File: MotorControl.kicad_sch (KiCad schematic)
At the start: 14 parts, among them J5 Conn_01x03_Pin, U3 CSD18534Q5A, U4 CSD18534Q5A, U5 CSD18534Q5A, U6 CSD18534Q5A, U7 CSD18534Q5A, U8 CSD18534Q5A, U9 DRV8323HRTAR

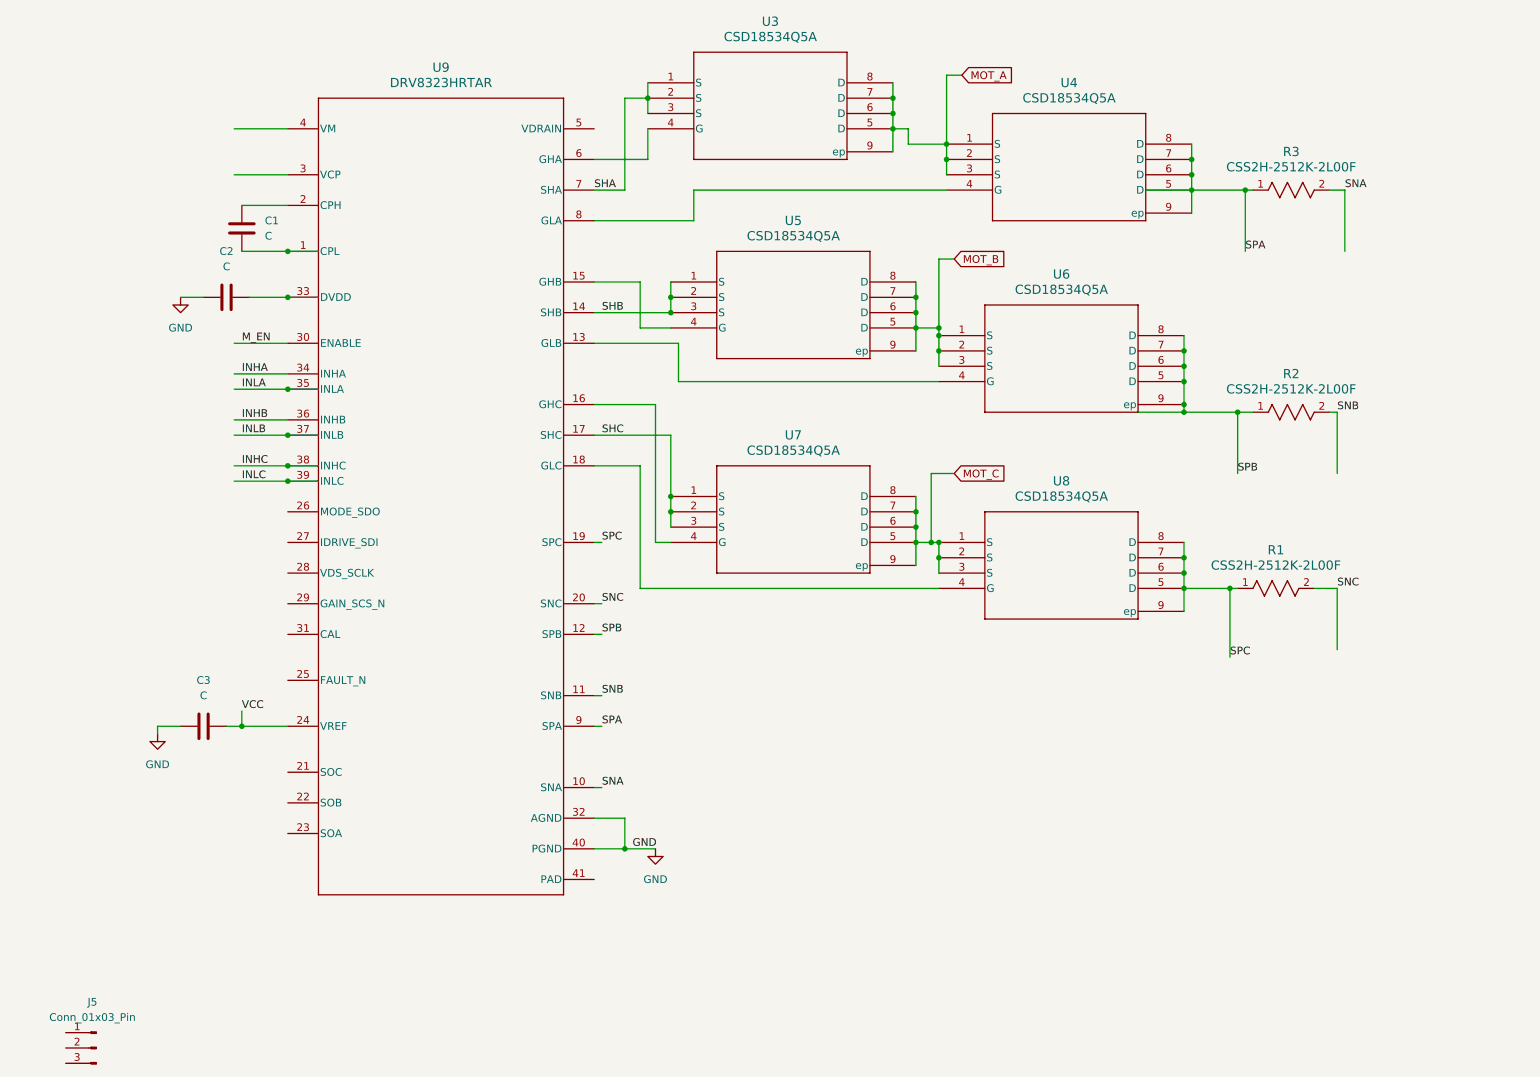
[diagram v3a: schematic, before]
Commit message: using vias on SNA/SPA instead of GxA b/c switching speed
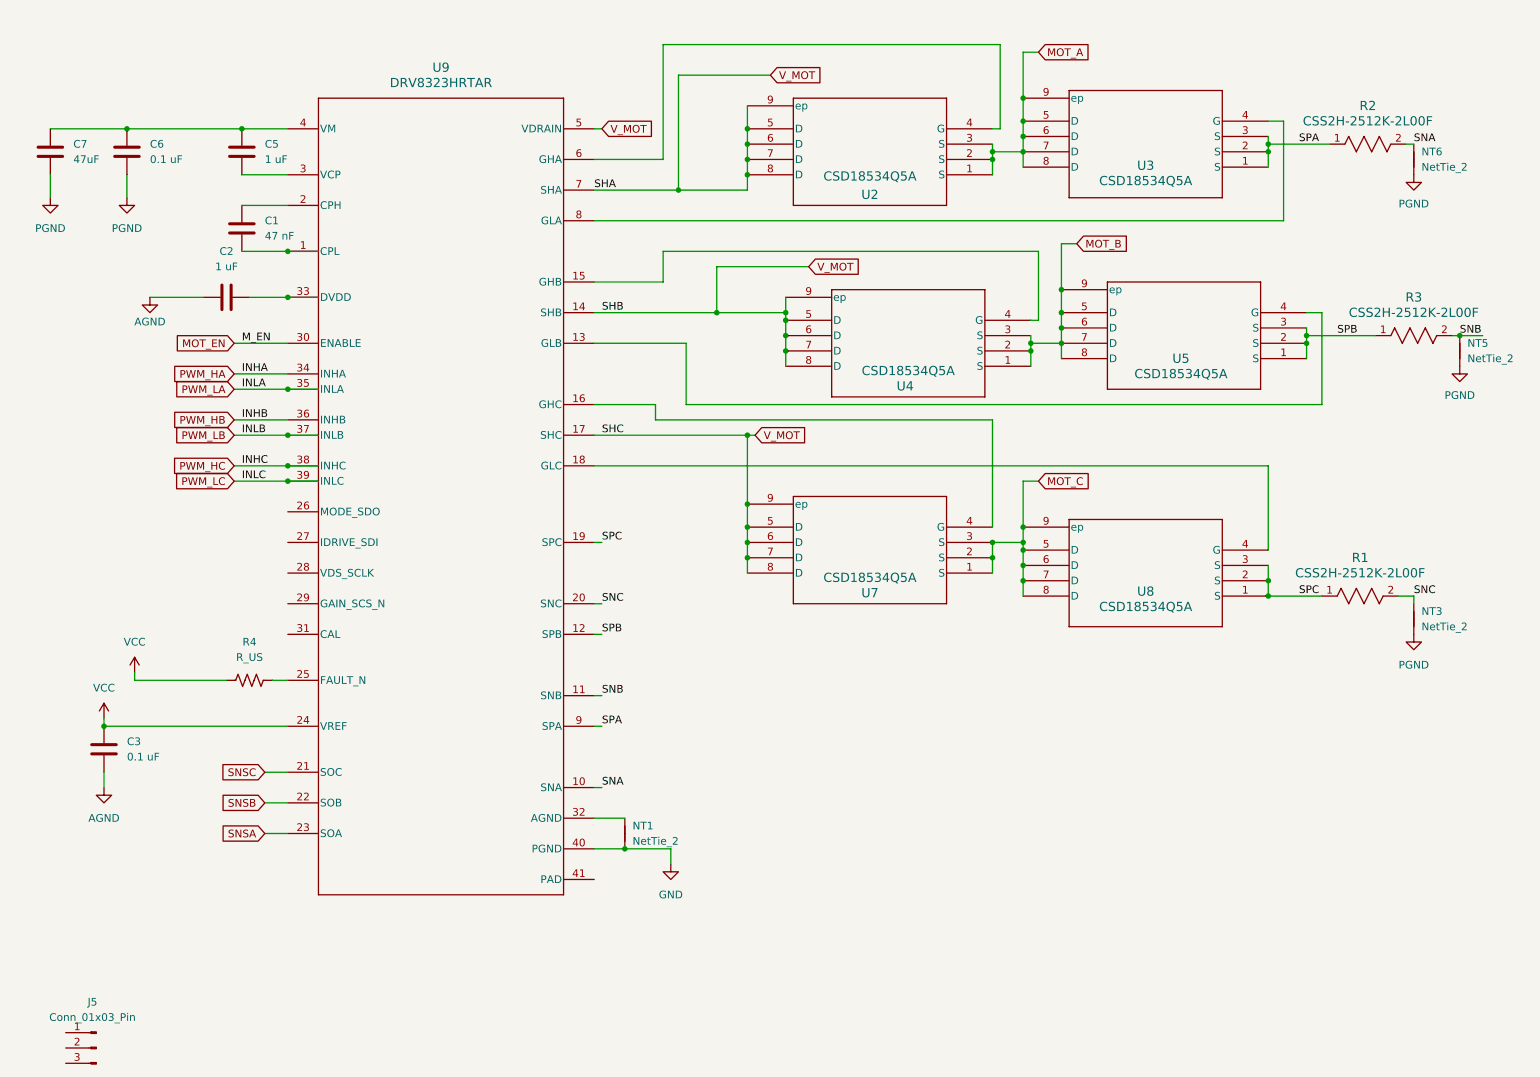
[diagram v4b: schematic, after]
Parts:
- removed U6: CSD18534Q5A, DQJ8, symbol CSD18534Q5A:CSD18534Q5A
- added C5: 1 uF, symbol Device:C
- added C6: 0.1 uF, symbol Device:C
- added C7: 47uF, symbol Device:C
- added NT1, NT3, NT5, NT6: NetTie_2, symbol Device:NetTie_2
- added R4: R_US, symbol Device:R_US
- added U2: CSD18534Q5A, DQJ8, symbol CSD18534Q5A:CSD18534Q5A
- C1: value C -> 47 nF
- C2: value C -> 1 uF
- C3: value C -> 0.1 uF
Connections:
- net GND: now also NT1.1; no longer C2.1, C3.1, U9.32 (AGND)
- net MOT_A: now also U2.1 (S), U2.2 (S), U2.3 (S); no longer U4.1 (S), U4.2 (S), U4.3 (S)
- net MOT_B: now also U4.1 (S), U4.2 (S), U4.3 (S)
- net MOT_C: now also U7.1 (S), U7.2 (S), U7.3 (S), U8.5 (D), U8.6 (D), U8.7 (D), U8.8 (D), U8.9 (ep); no longer U7.5 (D), U7.6 (D), U7.7 (D), U7.8 (D), U7.9 (ep), U8.1 (S), U8.2 (S), U8.3 (S)
- net SNA: now also R2.2, NT6.1; no longer R3.2
- net SNB: now also R3.2, NT5.1; no longer R2.2
- net SNC: now also NT3.1
- net SPA: now also R2.1, U3.1 (S), U3.2 (S), U3.3 (S); no longer R3.1, U4.5 (D), U4.6 (D), U4.7 (D), U4.8 (D), U4.9 (ep)
- net SPB: now also R3.1, U5.1 (S), U5.2 (S), U5.3 (S); no longer R2.1
- net SPC: now also U8.1 (S), U8.2 (S), U8.3 (S); no longer U8.5 (D), U8.6 (D), U8.7 (D), U8.8 (D), U8.9 (ep)
- net VCC: now also R4.1
- net at U5.4 (G): now also U9.13 (GLB); no longer U9.15 (GHB)
- net SNSC: now reaches U9.21 (SOC)
- net SNSB: now reaches U9.22 (SOB)
- net SNSA: now reaches U9.23 (SOA)
- net at U9.25 (FAULT_N): now also R4.2
- net at U9.3 (VCP): now also C5.2
- net at U9.4 (VM): now also C5.1, C6.1, C7.1
- net V_MOT: now reaches U9.5 (VDRAIN)
- net V_MOT: now also U4.5 (D), U4.6 (D), U4.7 (D), U4.8 (D), U4.9 (ep), U7.5 (D), U7.6 (D), U7.7 (D), U7.8 (D), U7.9 (ep), U9.14 (SHB), U9.17 (SHC), U9.7 (SHA), U2.5 (D), U2.6 (D), U2.7 (D), U2.8 (D), U2.9 (ep)
- net at U3.4 (G): now also U9.8 (GLA); no longer U9.6 (GHA)
- net at U4.4 (G): now also U9.15 (GHB); no longer U9.8 (GLA)
- net INHA renamed PWM_HA
- net INHB renamed PWM_HB
- net INHC renamed PWM_HC
- net INLA renamed PWM_LA
- net INLB renamed PWM_LB
- net INLC renamed PWM_LC
- net M_EN renamed MOT_EN
- removed net SHA: U3.1 (S), U3.2 (S), U3.3 (S), U9.7 (SHA)
- removed net SHB: U5.1 (S), U5.2 (S), U5.3 (S), U9.14 (SHB)
- removed net SHC: U7.1 (S), U7.2 (S), U7.3 (S), U9.17 (SHC)
- new net: NT1.2, U9.32 (AGND)
- new net: U2.4 (G), U9.6 (GHA)
- new net AGND: C2.1, C3.1
- new net PGND: C6.2, C7.2, NT3.2, NT5.2, NT6.2
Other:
- moved on the sheet: C3, R1, U7, U8

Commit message: full gate reroute with zones and sense lines like the layout guide
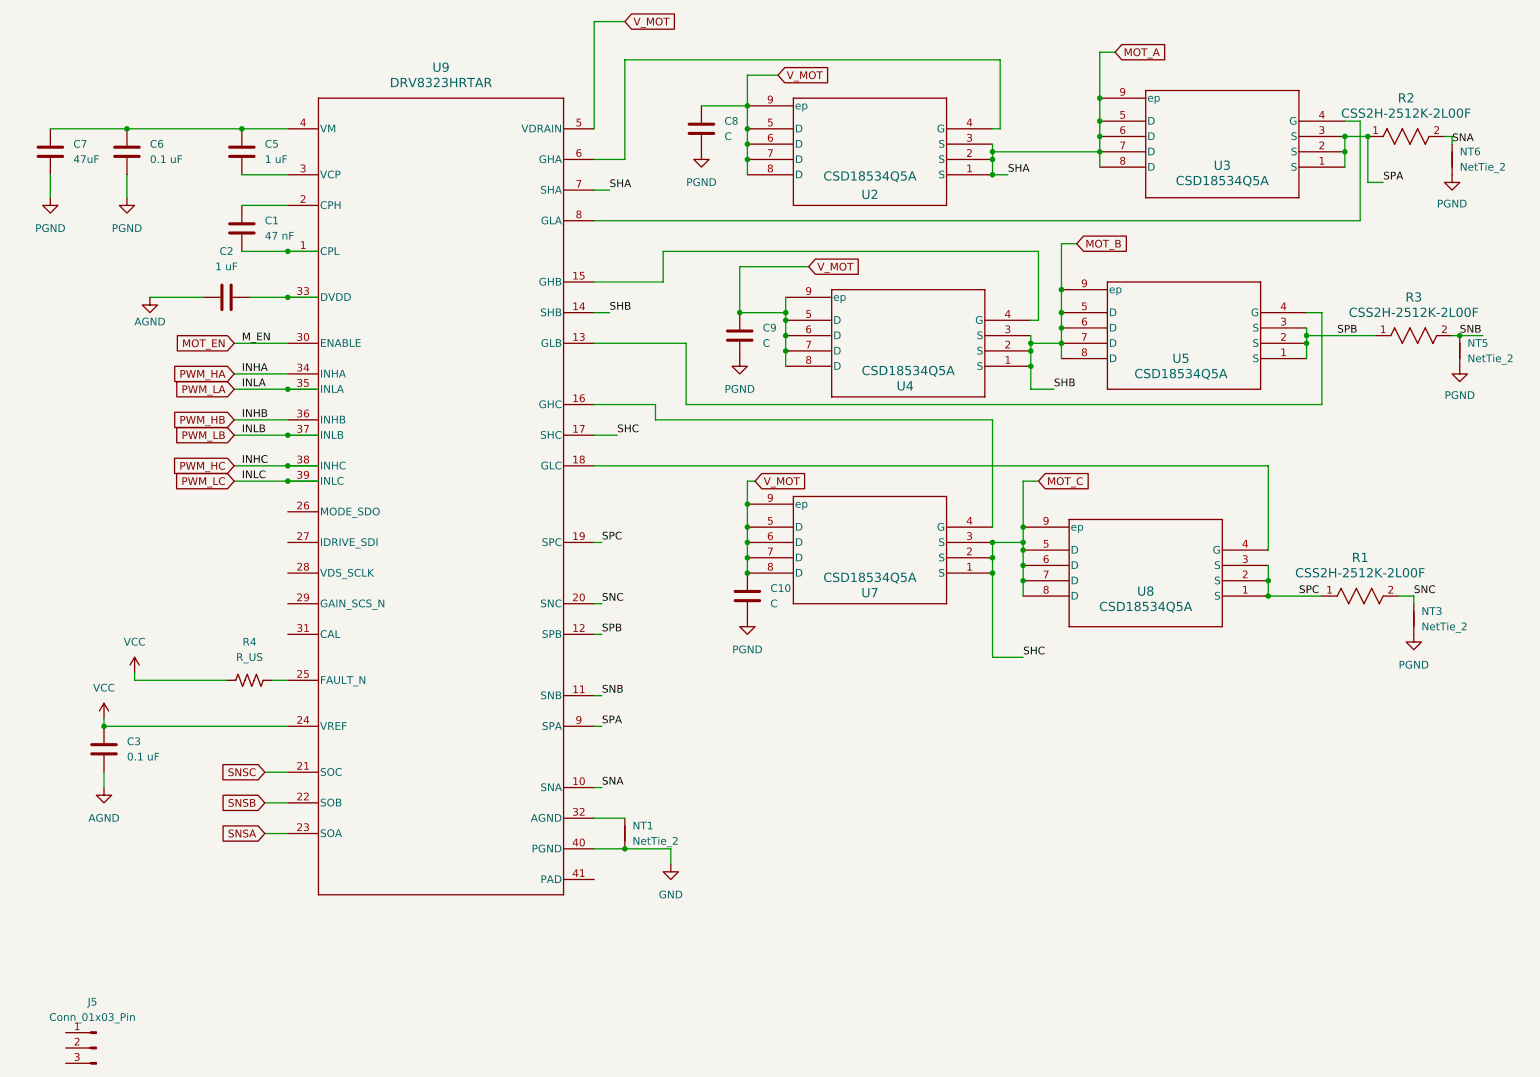
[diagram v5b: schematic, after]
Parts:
- added C10, C8, C9: C, symbol Device:C
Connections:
- net MOT_A: now also U9.7 (SHA)
- net MOT_B: now also U9.14 (SHB)
- net MOT_C: now also U9.17 (SHC)
- net PGND: now also C10.2, C8.1, C9.2
- net V_MOT: now also C10.1, C8.2, C9.1; no longer U9.14 (SHB), U9.17 (SHC), U9.7 (SHA)
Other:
- moved on the sheet: NT6, R2, U3

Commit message: selected mcu pins for sense in, SPI
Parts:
- removed J5: Conn_01x03_Pin, symbol Connector:Conn_01x03_Pin

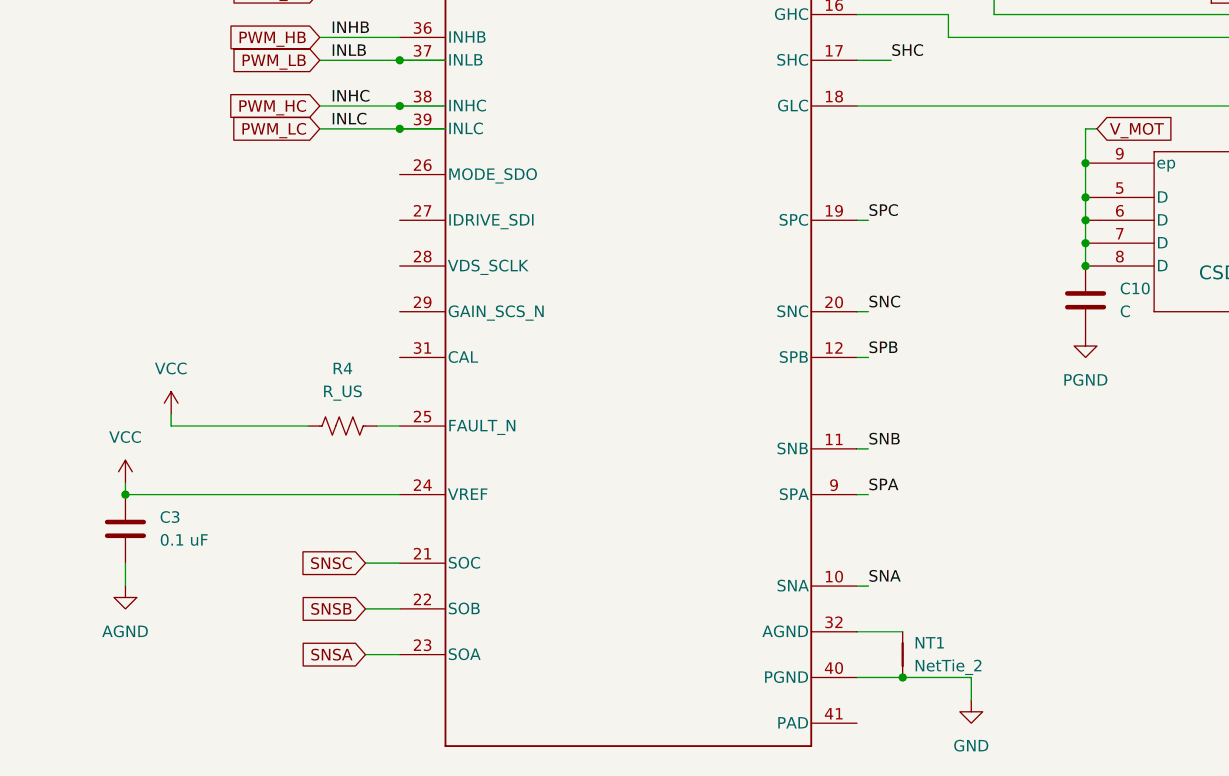
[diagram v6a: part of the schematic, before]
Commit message: big layout - lay pgnd and agnd zones and add SPI header pins
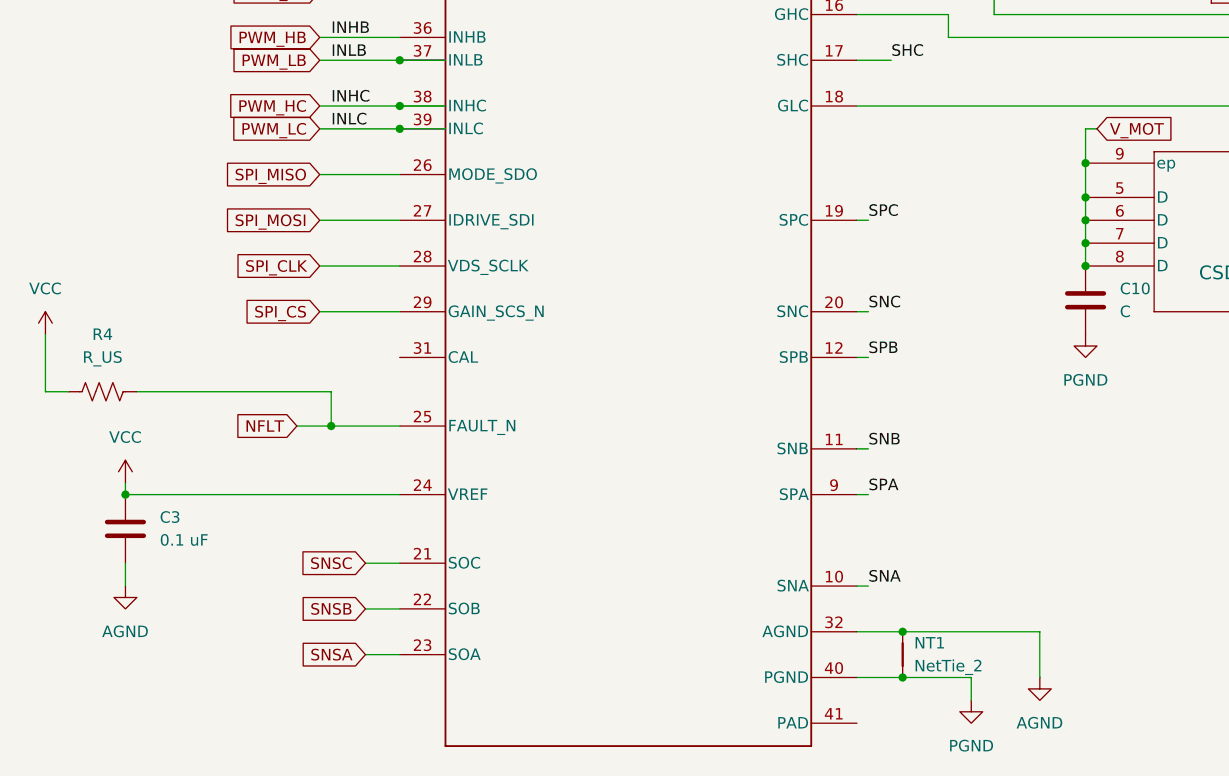
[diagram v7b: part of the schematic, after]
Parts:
- C1, C10, C2, C3, C5, C6, C8, C9: footprint (none) -> Capacitor_SMD:C_0805_2012Metric_Pad1.18x1.45mm_HandSolder
- R4: footprint (none) -> Resistor_SMD:R_0805_2012Metric_Pad1.20x1.40mm_HandSolder
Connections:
- net GND is gone; now on net PGND: NT1.1, U9.40 (PGND)
- net AGND: now also NT1.2, U9.32 (AGND)
- net NFLT: now reaches R4.2, U9.25 (FAULT_N)
- net SPI_MISO: now reaches U9.26 (MODE_SDO)
- net SPI_MOSI: now reaches U9.27 (IDRIVE_SDI)
- net SPI_CLK: now reaches U9.28 (VDS_SCLK)
- net SPI_CS: now reaches U9.29 (GAIN_SCS_N)
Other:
- moved on the sheet: R4
